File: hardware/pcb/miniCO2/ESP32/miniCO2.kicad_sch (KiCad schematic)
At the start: 25 parts, among them P1 USB_C_Plug_USB2.0, SW1 SW_Push, SW2 SW_Push, U1 ESP32-C6-MINI-1/U, U2 LM3281, U3 SCD40-D-R2, U4 SIT1552AI-JE-DCC-32.768D

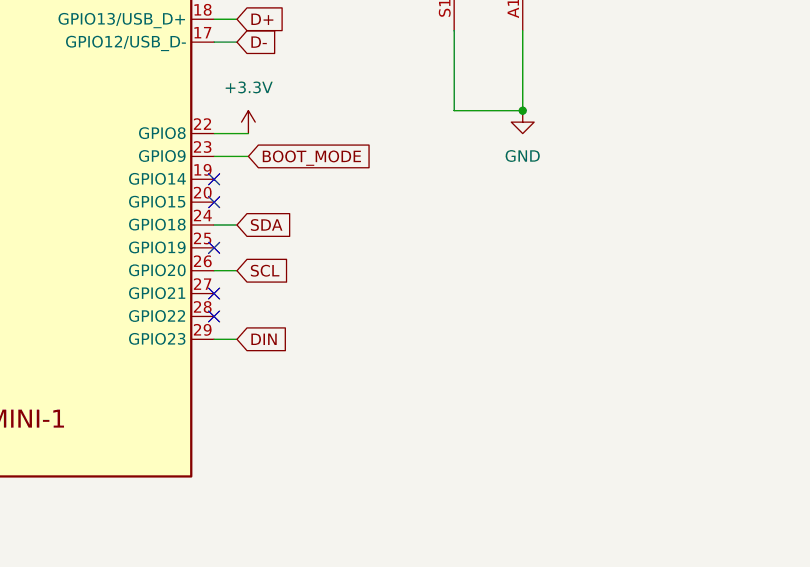
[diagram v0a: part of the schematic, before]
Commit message: scd40 centralization
Centralize SCD40 (shifted by 100um).
Bump version to 1b
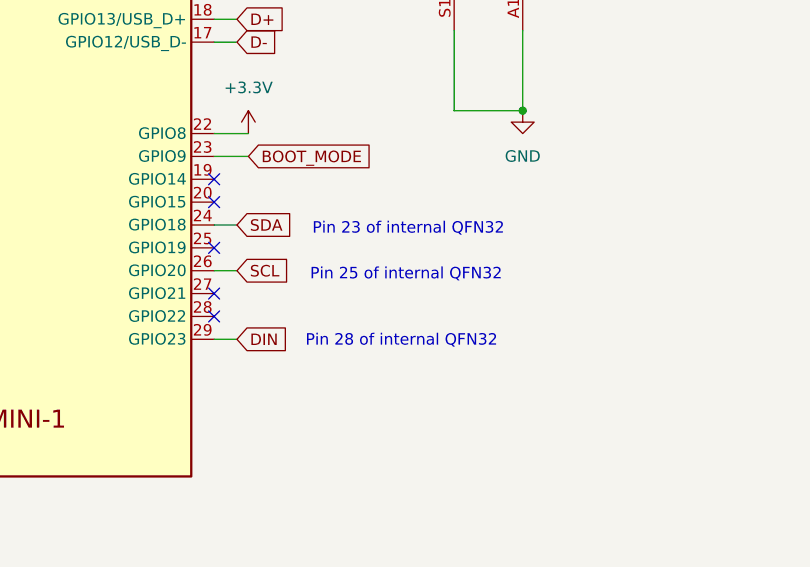
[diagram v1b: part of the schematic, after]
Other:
- note added: "Pin 23 of internal QFN32"
- note added: "Pin 25 of internal QFN32"
- note added: "Pin 28 of internal QFN32"
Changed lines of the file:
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@@
+		)
+	)
+	(text "Pin 23 of internal QFN32"
+		(exclude_from_sim no)
+		(at 200.66 83.058 0)
+		(effects
+			(font
+				(size 1.27 1.27)
+			)
+		)
+	)
+	(text "Pin 25 of internal QFN32"
+		(exclude_from_sim no)
+		(at 200.406 88.138 0)
+		(effects
+			(font
+				(size 1.27 1.27)
+			)
 		)
 	)
@@
 		(effects
 			(font
+				(size 1.27 1.27)
+			)
+		)
+	)
+	(text "Pin 28 of internal QFN32"
+		(exclude_from_sim no)
+		(at 199.898 95.504 0)
+		(effects
+			(font

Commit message: First commit of version 2
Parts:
- removed C1, C2, C3: 2.2uF, Capacitor_SMD:C_0201_0603Metric, symbol Device:C
- removed C5, C6: 22uF, Capacitor_SMD:C_0402_1005Metric, symbol Device:C
- removed C7: 100nF, Capacitor_SMD:C_0201_0603Metric, symbol Device:C
- removed D1: WS2812C-4020, miniCO2:WS2812C-4020, symbol MiniCO2:WS2812C-4020
- removed D2, D3: ESD9B3.3ST5G, Diode_SMD:D_SOD-923, symbol Diode:ESD9B3.3ST5G
- removed D4: ESD9B5.0ST5G, Diode_SMD:D_SOD-923, symbol Diode:ESD9B5.0ST5G
- removed F1: BSMD0402L-075, Capacitor_SMD:C_0402_1005Metric, symbol Device:Fuse
- removed L1: 0.47uH, Inductor_SMD:L_0603_1608Metric, symbol Device:L
- removed P1: USB_C_Plug_USB2.0, miniCO2:U261-121N-4BS2S, symbol Connector:USB_C_Plug_USB2.0
- removed R1, R4: 5.1k, Resistor_SMD:R_0201_0603Metric, symbol Device:R
- removed SW1: SW_Push, miniCO2:LS75C2D-T, symbol Switch:SW_Push
- removed U2: LM3281, Package_BGA:Texas_DSBGA-6_0.95x1.488mm_Layout2x3_P0.4mm, symbol MiniCO2:LM3281
- added D9: LED_green, LED_SMD:LED_0402_1005Metric, symbol Device:LED
- added R10, R9: 5.1k, Resistor_SMD:R_0201_0603Metric, symbol Device:R
- added U2: MAX809TEUR, Package_TO_SOT_SMD:SOT-23, symbol MiniCO2:MAX809
- C4: value 10uF -> 4.7uF/25V; LCSC Part # C85713 -> C69335; Temp range 10uF 10V -> (none)
- C8: value 22uF -> 100n; footprint Capacitor_SMD:C_0402_1005Metric -> Capacitor_SMD:C_0201_0603Metric; LCSC (none) -> C1525; LCSC Part # C3845593 -> C76934; MPN  (none) -> 100nF 10% 10V 0402; Temp range -55 to 85 -> (none)
- SW2: footprint miniCO2:LS75C2D-T -> miniCO2:GT-TC108X-H034; LCSC Part # C962551 -> C22396279
- U1: LCSC Part # C5736265 -> C5736265
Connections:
- net +3.3V: now also U2.3 (VCC)
- net BOOT_MODE: now also C8.1, R9.1; no longer SW2.2
- net EN: now also U2.2 (~{RESET})
- net GND: now also C8.2, D9.1 (K), U2.1 (GND); no longer C8.1
- net VBUS_EN_SENSE: now reaches U1.10 (MTDI/GPIO5/ADC1_CH5)
- net CHRG_SENSE: now reaches U1.13 (GPIO1/ADC1_CH1/XTAL_32K_N)
- net SPISCL: now reaches U1.15 (MTCK/GPIO6/ADC1_CH6)
- net MOSI: now reaches U1.16 (MTDO/GPIO7)
- net CS#: now reaches U1.25 (GPIO19)
- net at U1.27 (GPIO21): now also R10.2
- net BUSY: now reaches U1.5 (GPIO2/ADC1_CH2)
- net RES#: now reaches U1.6 (GPIO3/ADC1_CH3)
- net D/C#: now reaches U1.9 (MTMS/GPIO4/ADC1_CH4)
- net DIN: no longer names the net of U1.29 (GPIO23)
- new net: R9.2, SW2.2
- new net: D9.2 (A), R10.1
- no-connect marks 16 -> 6
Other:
- added sheet Display (display.kicad_sch)
- added sheet Input and power (untitled.kicad_sch)
- note removed: "Pin 28 of internal QFN32"
- moved on the sheet: R6, R7, SW2, U1, U3

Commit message: Modifications before sending to production
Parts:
- C4: value 4.7uF/25V -> 4.7uF/35V; LCSC Part # C69335 -> C162274
- C8: value 100n -> 100n/25V; LCSC C1525 -> (none); LCSC Part # C76934 -> C181047
- D9: LCSC Part # C2898985 -> C5336761
- R10, R6, R7, R9: LCSC Part # C274341 -> C270344
- U3: value SCD40-D-R2 -> SCD40; LCSC Part # C3659421 -> C3037696
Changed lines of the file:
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@@
 			)
 		)
-		(property "LCSC Part #" "C274341"
+		(property "LCSC Part #" "C270344"
 			(at 64.77 39.37 0)
 			(effects
@@
 			)
 		)
-		(property "Datasheet" "https://www.lcsc.com/datasheet/lcsc_datasheet_2109221830_ROHM-Semicon-SML-P13PTT86R_C2898985.pdf"
+		(property "Datasheet" "https://www.lcsc.com/datasheet/lcsc_datasheet_2411291500_ROHM-Semicon-SML-P11MTT86R_C5336761.pdf"
 			(at 167.64 106.68 0)
 			(effects
@@
 			)
 		)
-		(property "LCSC Part #" "C2898985"
+		(property "LCSC Part #" "C5336761"
 			(at 167.64 106.68 90)
 			(effects
@@
 			)
 		)
-		(property "Value" "100n"
+		(property "Value" "100n/25V"
 			(at 62.738 140.208 0)
 			(effects
@@
 			)
 		)
-		(property "LCSC" "C1525"
+		(property "LCSC" ""
 			(at 59.69 138.43 0)
 			(effects
@@
 			)
 		)
-		(property "LCSC Part #" "C76934"
+		(property "LCSC Part #" "C181047"
 			(at 59.69 138.43 0)
 			(effects
@@
 			)
 		)
-		(property "Value" "4.7uF/25V"
+		(property "Value" "4.7uF/35V"
 			(at 115.062 39.37 0)
 			(effects
@@
 			)
 		)
-		(property "LCSC Part #" "C69335"
+		(property "LCSC Part #" "C162274"
 			(at 128.27 38.1 0)
 			(effects
@@
 			)
 		)
-		(property "LCSC Part #" "C274341"
+		(property "LCSC Part #" "C270344"
 			(at 55.88 39.37 0)
 			(effects
@@
 			)
 		)
-		(property "LCSC Part #" "C274341"
+		(property "LCSC Part #" "C270344"
 			(at 167.64 99.06 0)
 			(effects
@@
 			)
 		)
-		(property "LCSC Part #" "C274341"
+		(property "LCSC Part #" "C270344"
 			(at 54.61 133.35 0)
 			(effects
@@
 			)
 		)
-		(property "Value" "SCD40-D-R2"
+		(property "Value" "SCD40"
 			(at 58.928 32.766 0)
 			(effects
@@
 			)
 		)
-		(property "LCSC Part #" "C3659421"
+		(property "LCSC Part #" "C3037696"
 			(at 44.45 46.99 0)
 			(effects
